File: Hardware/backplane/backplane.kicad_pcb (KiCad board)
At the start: 2 copper layers, 99.9 x 99.9 mm, 62 parts, among them J1 USB_B_Micro, J2 Conn_02x02_Odd_Even, SW1 SW_SPST, U1 74AC161, U2 MAX811SEUS-T, U3 MAX811SEUS-T, U4 PAL24, X1 24MHz

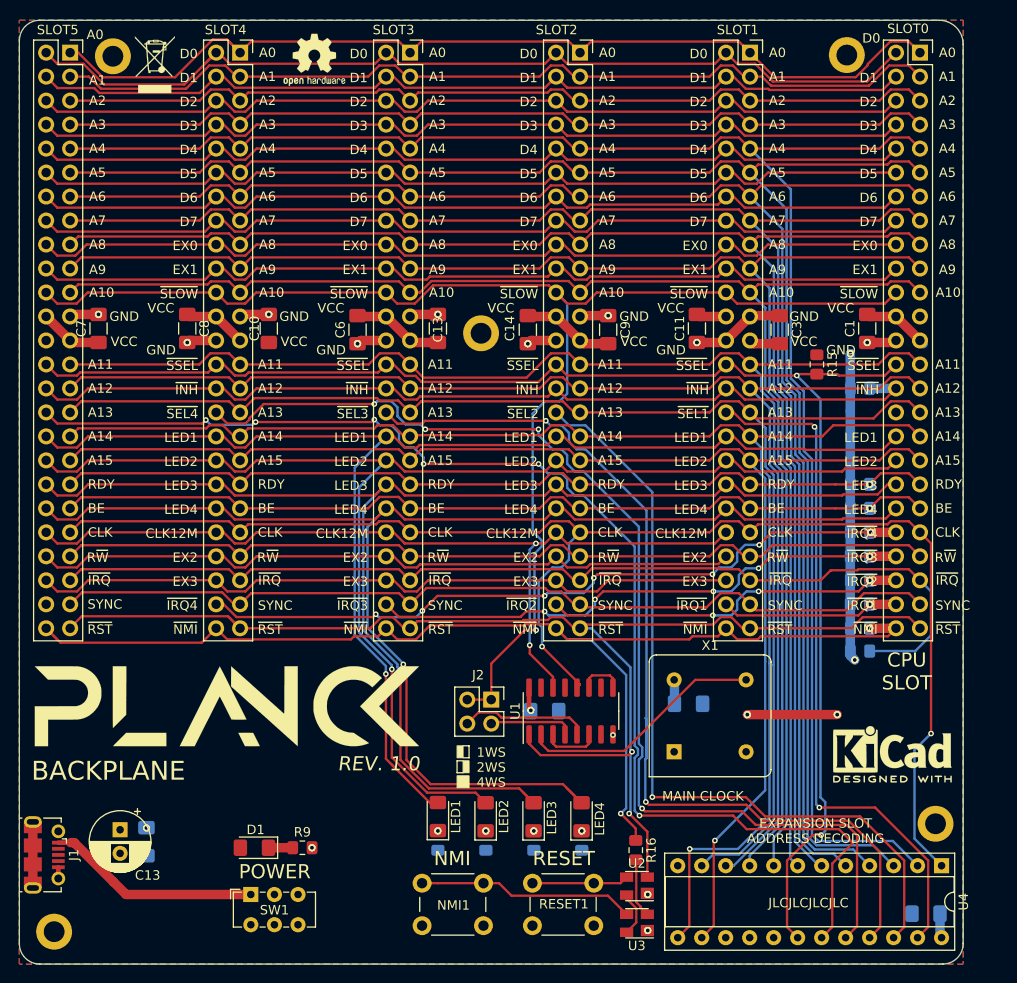
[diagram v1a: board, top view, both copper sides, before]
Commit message: Add IRQ signal for Slot 5
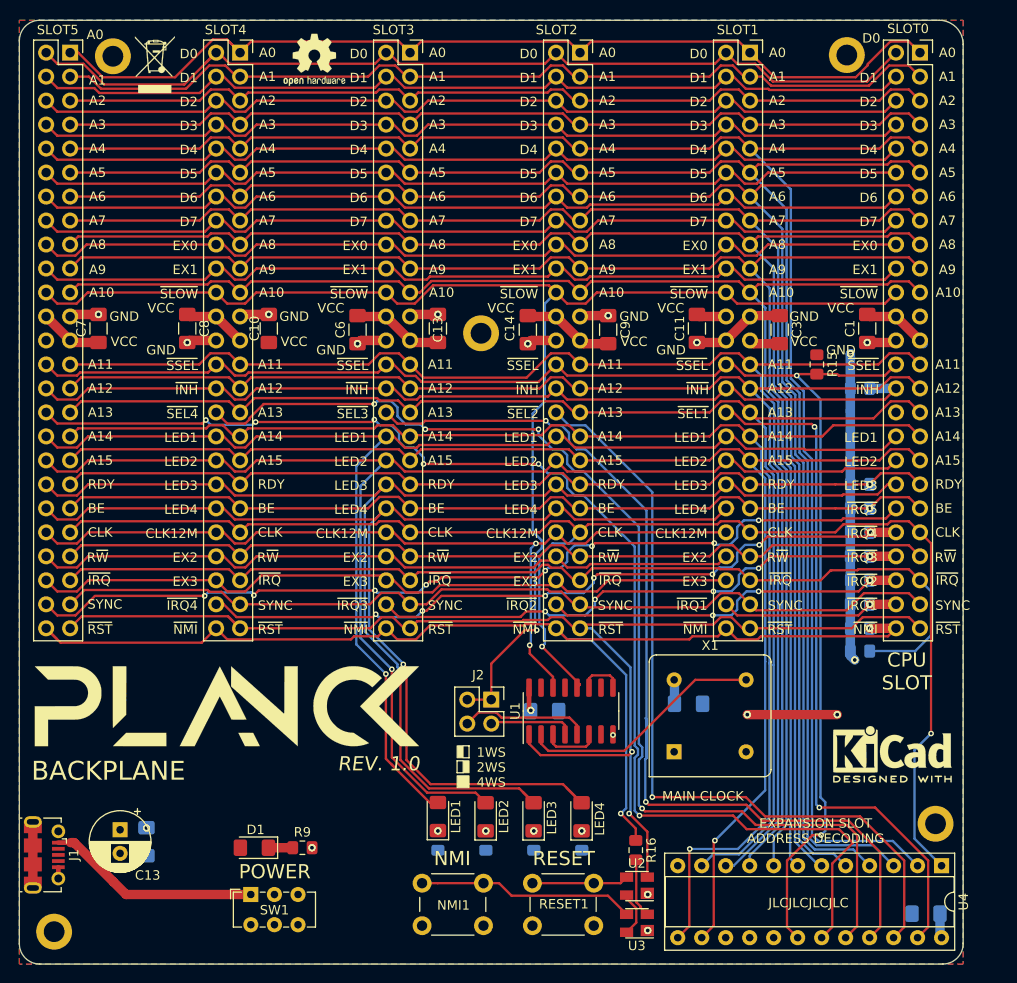
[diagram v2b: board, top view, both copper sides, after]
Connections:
- SLOT0 pad 40: LED4 -> ~IRQ5~
- SLOT5 pad 48: Net-(SLOT5-Pad48) -> ~IRQ5~
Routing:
- net ~IRQ5~: track 0.00 -> 97.1 mm, vias 0 -> 8
- net LED4: track 146.7 -> 128.4 mm
- net ~SLOW~: track 147.9 -> 146.0 mm
- net CLK: track 153.3 -> 154.0 mm
- net EX3: track 75.9 -> 76.4 mm
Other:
- board text added: "~IRQ5~"

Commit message: Backplane provides diode and pullups for SLOW signal
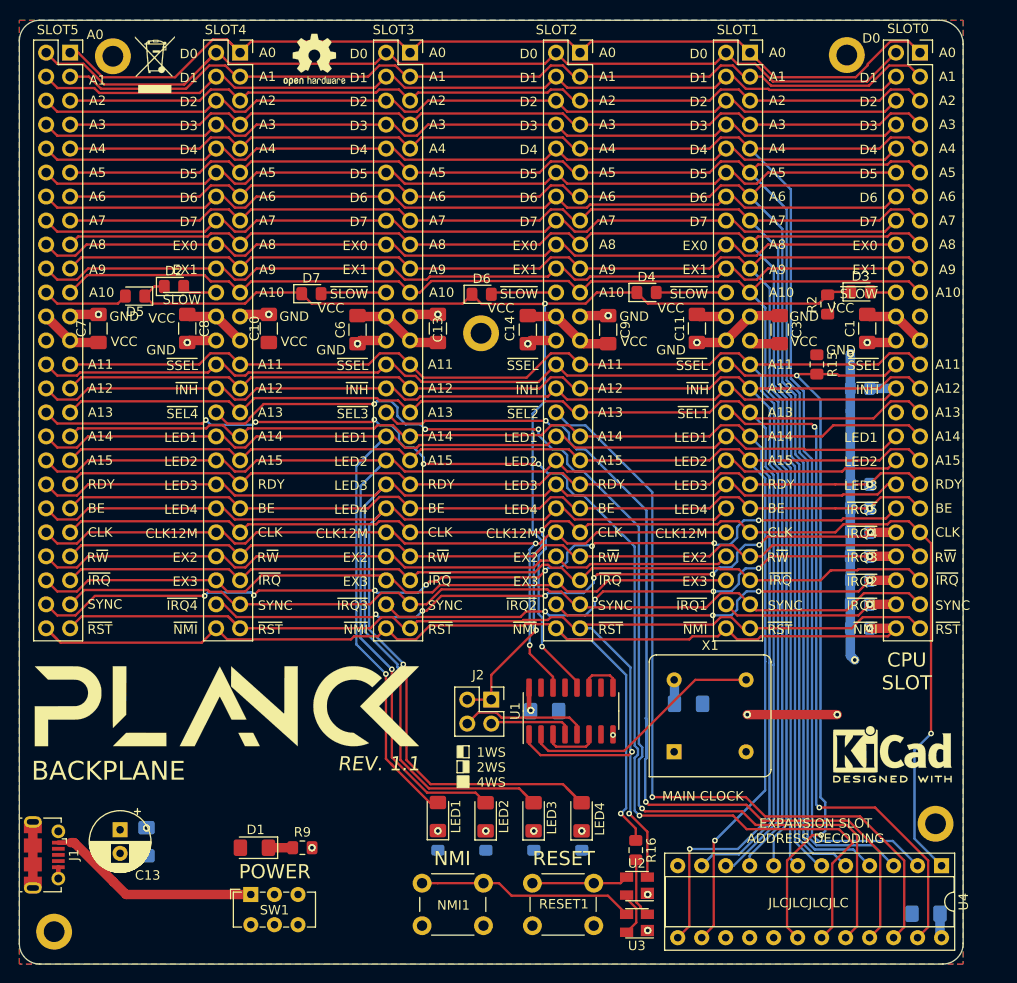
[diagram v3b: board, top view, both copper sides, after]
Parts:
- added D2: DIODE, Diode_SMD:D_0805_2012Metric_Pad1.15x1.40mm_HandSolder, F.Cu at (16.4, 28.2)
- added D3: DIODE, Diode_SMD:D_0805_2012Metric_Pad1.15x1.40mm_HandSolder, F.Cu at (89.1, 28.8)
- added D4: DIODE, Diode_SMD:D_0805_2012Metric_Pad1.15x1.40mm_HandSolder, F.Cu at (66.4, 28.8)
- added D5: DIODE, Diode_SMD:D_0805_2012Metric_Pad1.15x1.40mm_HandSolder, F.Cu at (12.3, 29.2)
- added D6: DIODE, Diode_SMD:D_0805_2012Metric_Pad1.15x1.40mm_HandSolder, F.Cu at (49.0, 29.0)
- added D7: DIODE, Diode_SMD:D_0805_2012Metric_Pad1.15x1.40mm_HandSolder, F.Cu at (30.9, 29.0)
- R2: moved to F.Cu
- moved R2 36.9 mm to (85.6, 30.1), turned to 90 degrees
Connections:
- R2 pad 2: ~IRQ~ -> ~SLOW~
- SLOT0 pad 22: ~SLOW~ -> Net-(D3-Pad2)
- SLOT1 pad 22: ~SLOW~ -> Net-(D4-Pad2)
- SLOT2 pad 22: ~SLOW~ -> Net-(D6-Pad2)
- SLOT3 pad 22: ~SLOW~ -> Net-(D7-Pad2)
- SLOT4 pad 22: ~SLOW~ -> Net-(D2-Pad2)
- SLOT5 pad 22: ~SLOW~ -> Net-(D5-Pad2)
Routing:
- net ~SLOW~: track 146.0 -> 128.7 mm, vias 1 -> 2
- net ~IRQ~: track 108.9 -> 95.4 mm
- net Net-(D5-Pad2): track 0.00 -> 9.21 mm
- net Net-(D4-Pad2): track 0.00 -> 7.39 mm
- net Net-(D7-Pad2): track 0.00 -> 6.94 mm
- net Net-(D6-Pad2): track 0.00 -> 6.93 mm
- net Net-(D2-Pad2): track 0.00 -> 4.06 mm
- net Net-(D3-Pad2): track 0.00 -> 2.75 mm
- net CLK: track 154.0 -> 151.4 mm, vias 2 -> 3
- net A10: track 157.8 -> 158.3 mm
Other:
- board text added: "REV. 1.1"

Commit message: small fixes on the hardware
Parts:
- removed the REF** at (48.9, 33.1)
- removed the REF** at (3.68, 96.5)
- removed the REF** at (9.91, 3.81)
- removed the REF** at (87.6, 3.68)
- removed the REF** at (97.0, 85.1)
- added H1: MountingHole_Pad, MountingHole:MountingHole_3.2mm_M3_Pad, F.Cu at (86.7, 3.81)
- added H2: MountingHole_Pad, MountingHole:MountingHole_3.2mm_M3_Pad, F.Cu at (4.06, 95.9)
- added H3: MountingHole_Pad, MountingHole:MountingHole_3.2mm_M3_Pad, F.Cu at (10.8, 3.81)
- added H4: MountingHole_Pad, MountingHole:MountingHole_3.2mm_M3_Pad, F.Cu at (96.1, 83.3)
- added R17: 1k, Resistor_SMD:R_0805_2012Metric_Pad1.15x1.40mm_HandSolder, F.Cu at (43.5, 76.8)
- added R18: 1k, Resistor_SMD:R_0805_2012Metric_Pad1.15x1.40mm_HandSolder, F.Cu at (43.5, 74.6)
- moved REF** 17.9 mm to (31.1, 11.0)
- moved C4 2.86 mm to (70.9, 75.2)
- moved X1 2.86 mm to (69.3, 80.3)
- moved REF** 2.61 mm to (92.3, 75.1)
- moved J1 1.46 mm to (2.73, 86.9)
- moved G*** 0.76 mm to (21.4, 73.2)
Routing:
- net /DS1: track 8.99 -> 15.5 mm
- net CLK: track 151.4 -> 156.0 mm
- net A0: track 101.1 -> 104.4 mm
- net /DS2: track 13.6 -> 16.6 mm
- net D0: track 100.2 -> 102.5 mm
- net A1: track 96.7 -> 99.0 mm
- net D1: track 95.5 -> 97.8 mm
- net A2: track 94.9 -> 96.3 mm
- net Net-(J1-Pad1): track 23.4 -> 24.8 mm
- net /CLK_24M: track 26.1 -> 24.9 mm
